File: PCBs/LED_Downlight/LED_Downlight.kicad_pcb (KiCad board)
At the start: 2 copper layers, 6 parts, among them J1 Conn_01x02_Female, J2 Conn_01x02_Female

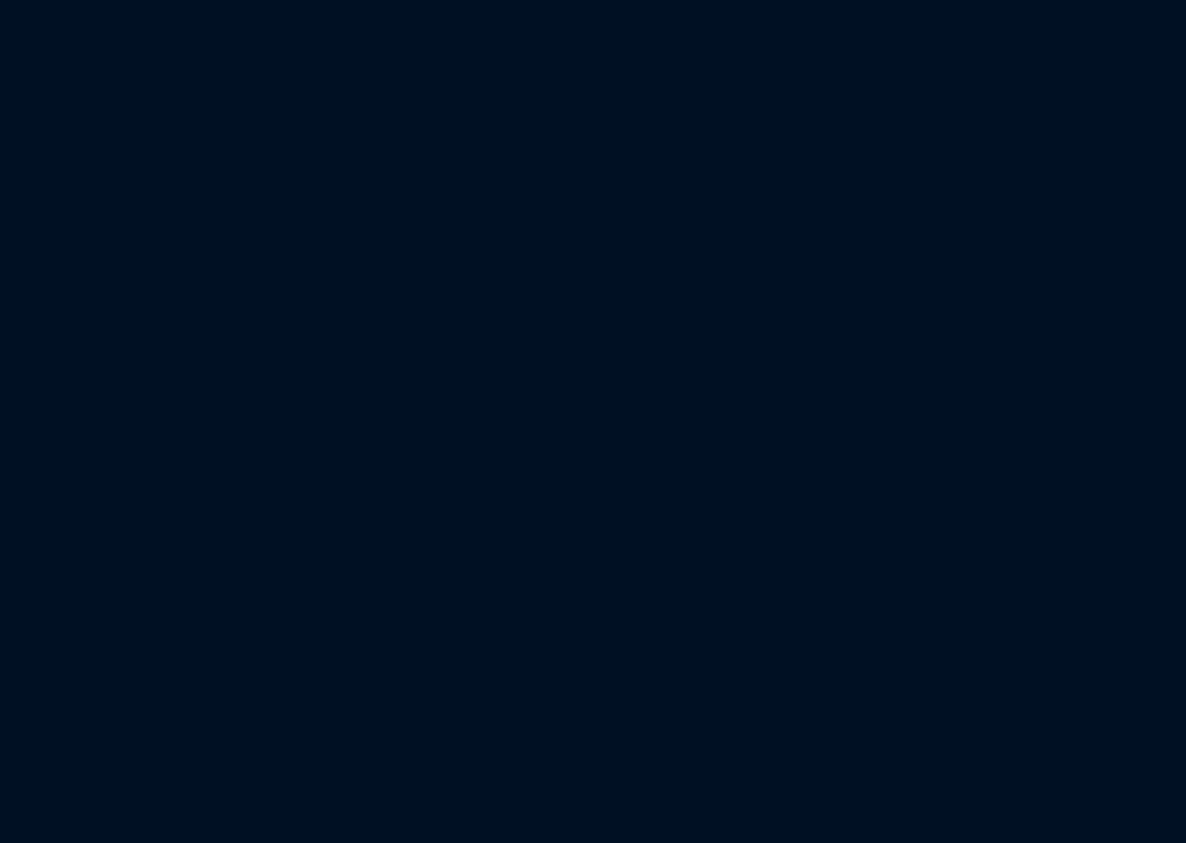
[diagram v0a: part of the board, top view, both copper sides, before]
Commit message: Tactile Switch
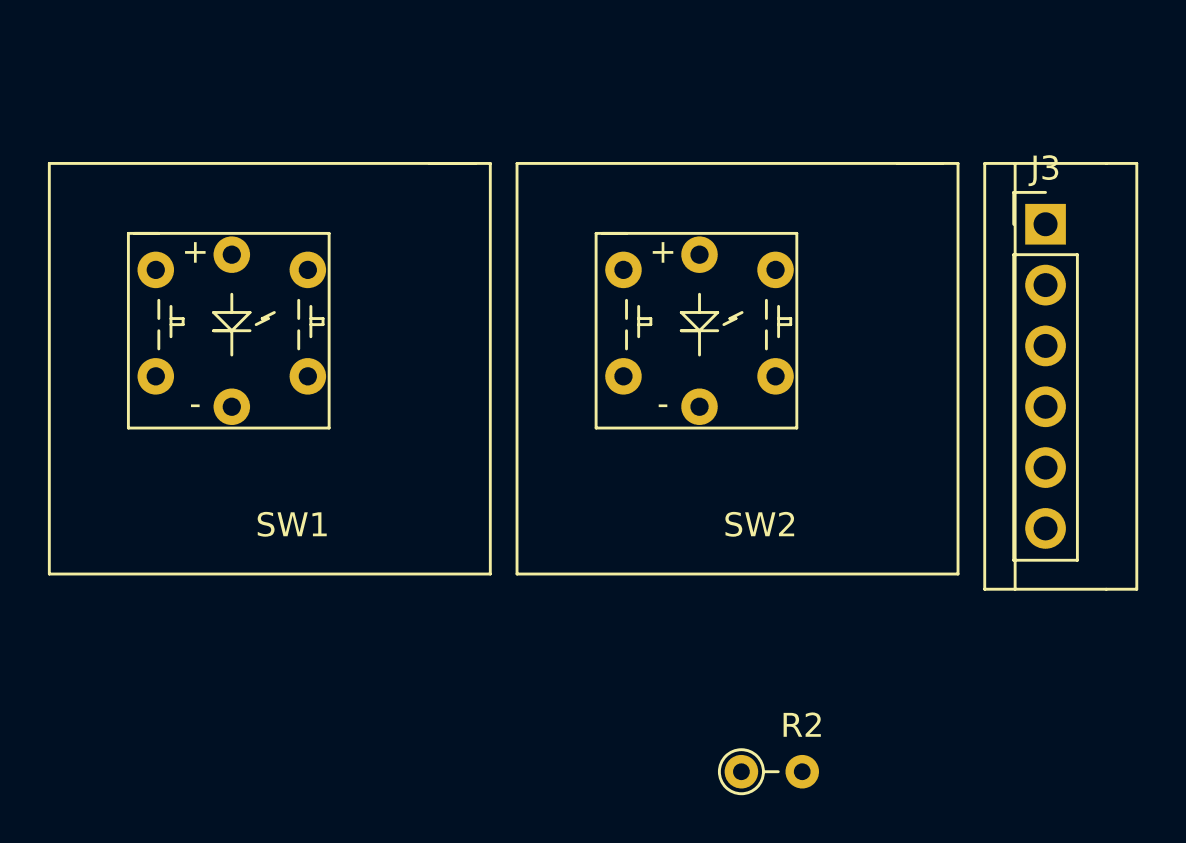
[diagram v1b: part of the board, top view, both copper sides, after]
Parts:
- added J3: PT_Conn_01x06, PT_Library_v001:PT_PinHeader_1x06_P2.54mm_Vertical, F.Cu at (165.1, 101.6)
- added R2: R_US, PT_Library_v001:PT_R_Axial_DIN0204_L3.6mm_D1.6mm_P2.54mm_Vertical, F.Cu at (152.4, 124.5)
- added SW1: PT_Tactile_Switch_Led, PT_Library_v001:PT_Small_Tactile_Switch_With_LED, F.Cu at (133.7, 113.7)
- added SW2: PT_Tactile_Switch_Led, PT_Library_v001:PT_Small_Tactile_Switch_With_LED, F.Cu at (153.2, 113.7)

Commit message: LED Downlight
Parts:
- removed J3: PT_Conn_01x06, PT_Library_v001:PT_PinHeader_1x06_P2.54mm_Vertical
- removed SW1, SW2: PT_Tactile_Switch_Led, PT_Library_v001:PT_Small_Tactile_Switch_With_LED
- added D4: LED, LED_THT:LED_D8.0mm, F.Cu at (182.8, 52.3)
- added D5: LED, LED_THT:LED_D8.0mm, F.Cu at (193.5, 52.3)
- added D6: LED, LED_THT:LED_D8.0mm, F.Cu at (204.2, 52.3)
- added H1: MountingHole, MountingHole:MountingHole_3.2mm_M3, F.Cu at (170.7, 48.9)
- added H2: MountingHole, MountingHole:MountingHole_3.2mm_M3, F.Cu at (214.3, 49.5)
- added H3: MountingHole, MountingHole:MountingHole_3.2mm_M3, F.Cu at (170.4, 70.1)
- added H4: MountingHole, MountingHole:MountingHole_3.2mm_M3, F.Cu at (214.3, 70.1)
- added H5: MountingHole, MountingHole:MountingHole_3.2mm_M3, F.Cu at (193.9, 59.8)
- D1: footprint PT_Library_v001:PT_PinHeader_1x08_P2.54mm_Vertical -> LED_THT:LED_D8.0mm
- D2, D3: footprint PT_Library_v001:PT_CP_Radial_D8.0mm_P2.50mm -> LED_THT:LED_D8.0mm
- J1, J2: value Conn_01x02_Female -> Conn_01x04_Female; footprint PT_Library_v001:PT_R_Axial_DIN0204_L3.6mm_D1.6mm_P2.54mm_Vertical -> Connector_PinHeader_2.54mm:PinHeader_1x04_P2.54mm_Horizontal; moved to B.Cu
- R1: footprint PT_Library_v001:PT_CP_Radial_D8.0mm_P2.50mm -> PT_Library_v001:R_Axial_DIN0207_L6.3mm_D2.5mm_P7.62mm_Horizontal; moved to B.Cu
- R2: footprint PT_Library_v001:PT_R_Axial_DIN0204_L3.6mm_D1.6mm_P2.54mm_Vertical -> PT_Library_v001:R_Axial_DIN0207_L6.3mm_D2.5mm_P7.62mm_Horizontal; moved to B.Cu
- moved J2 80.5 mm to (210.3, 63.8)
- moved R2 71.7 mm to (178.9, 57.8)
- moved D3 58.7 mm to (204.7, 70.0), turned to 90 degrees
- moved D2 57.6 mm to (193.9, 70.0), turned to 90 degrees
- moved D1 55.0 mm to (183.2, 69.9), turned to 90 degrees
- moved R1 48.3 mm to (179.3, 61.6)
- moved J1 40.9 mm to (176.6, 55.8), turned to 180 degrees
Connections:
- net Net-(D3-Pad1) renamed /GNDGreen
- net Net-(J1-Pad1) renamed /+12VGreen
- R2 pad 1: Net-(R2-Pad1) -> /+12VWhite
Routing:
- net /GNDGreen: track 0.00 -> 46.6 mm
- net /+12VGreen: track 0.00 -> 40.9 mm
- net /GNDWhite: track 0.00 -> 40.2 mm
- net /+12VWhite: track 0.00 -> 36.8 mm
- net Net-(D2-Pad1): track 0.00 -> 11.9 mm
- net Net-(D5-Pad1): track 0.00 -> 11.8 mm
- net Net-(D4-Pad1): track 0.00 -> 11.8 mm
- net Net-(D1-Pad1): track 0.00 -> 11.7 mm
- net Net-(D4-Pad2): track 0.00 -> 9.66 mm
- net Net-(D1-Pad2): track 0.00 -> 7.29 mm
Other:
- net class Power added: clearance 0.2, trace_width 0.5, via_dia 0.8, via_drill 0.4
- board text added: "Green LEDs"
- board text added: "White LED"
